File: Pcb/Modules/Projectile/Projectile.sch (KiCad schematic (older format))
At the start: 29 parts, among them J1 JACK_RJ45, Q1 Q_NMOS_GSD, U1 OPA320, U2 OPA320

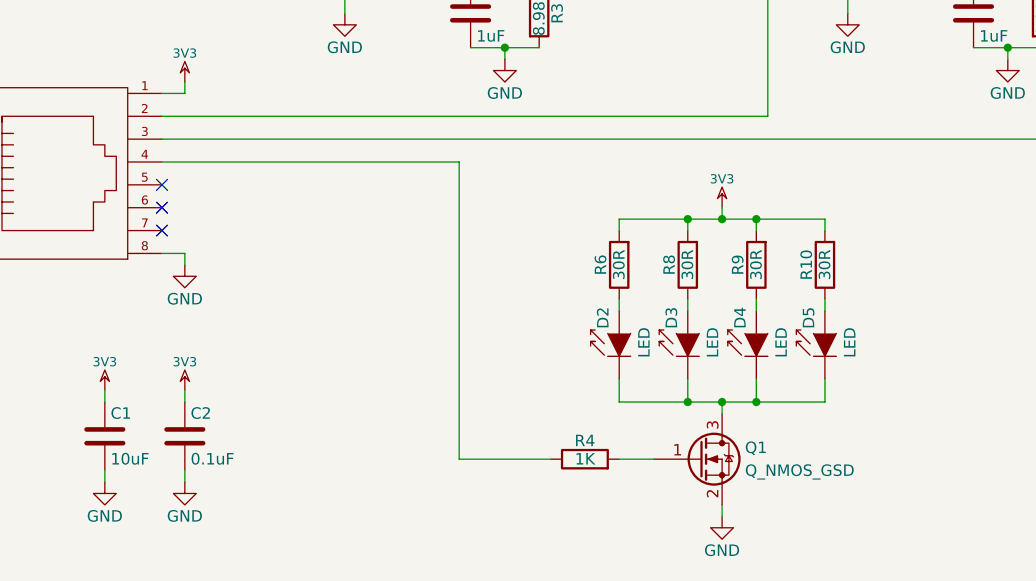
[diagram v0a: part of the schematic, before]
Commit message: Pcb layout for beam and projectile module
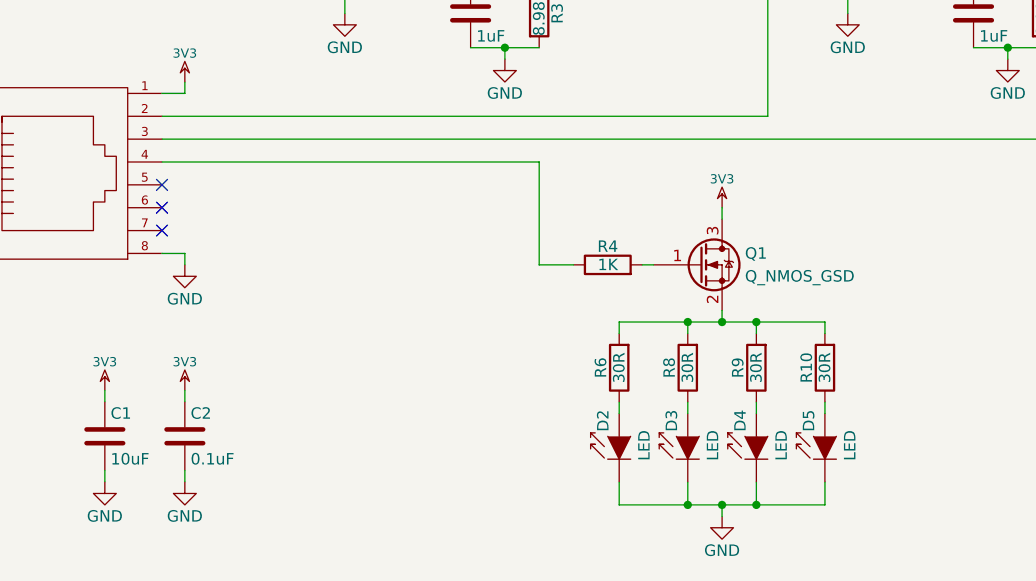
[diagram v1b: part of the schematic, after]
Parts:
- U1, U2: footprint (none) -> TO_SOT_Packages_SMD:SOT-23-5
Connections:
- net 3V3: now also Q1.3 (D); no longer R10.2, R6.2, R8.2, R9.2
- net GND: now also D2.1 (K), D3.1 (K), D4.1 (K), D5.1 (K); no longer Q1.2 (S)
- new net: Q1.2 (S), R10.2, R6.2, R8.2, R9.2
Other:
- moved on the sheet: D2, D3, D4, D5, Q1, R10, R4, R6, R8, R9

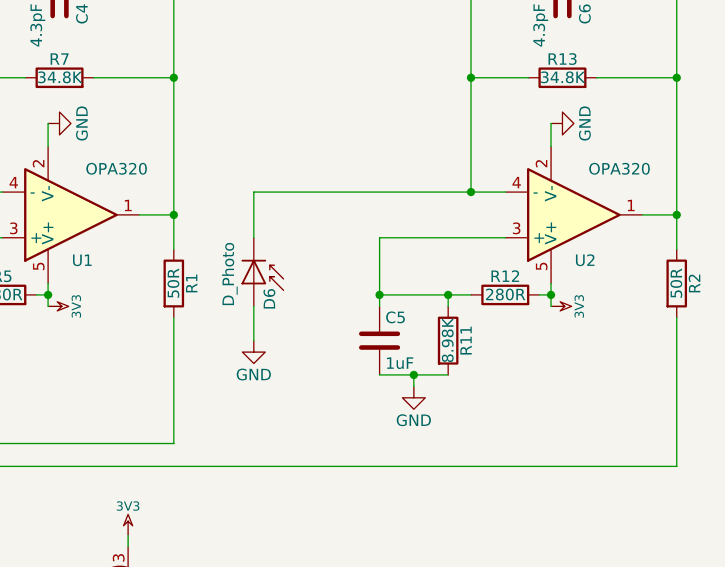
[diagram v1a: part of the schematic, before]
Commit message: Change 50 ohm resistor to 49.9
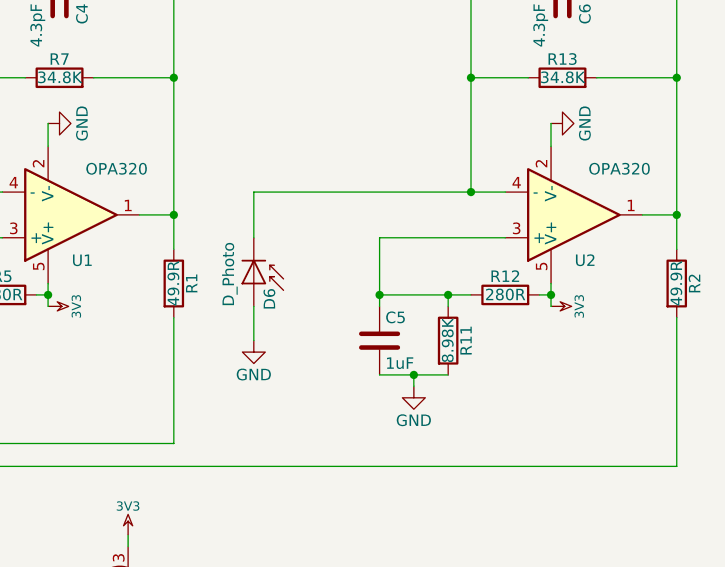
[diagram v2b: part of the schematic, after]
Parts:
- R1, R2: value 50R -> 49.9R
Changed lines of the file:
@@
 P 5300 3200
 F 0 "R1" V 5380 3200 50  0000 C CNN
-F 1 "50R" V 5300 3200 50  0000 C CNN
+F 1 "49.9R" V 5300 3200 50  0000 C CNN
 F 2 "Resistors_SMD:R_0603" V 5230 3200 50  0001 C CNN
 F 3 "" H 5300 3200 50  0001 C CNN
@@
 P 7500 3200
 F 0 "R2" V 7580 3200 50  0000 C CNN
-F 1 "50R" V 7500 3200 50  0000 C CNN
+F 1 "49.9R" V 7500 3200 50  0000 C CNN
 F 2 "Resistors_SMD:R_0603" V 7430 3200 50  0001 C CNN
 F 3 "" H 7500 3200 50  0001 C CNN

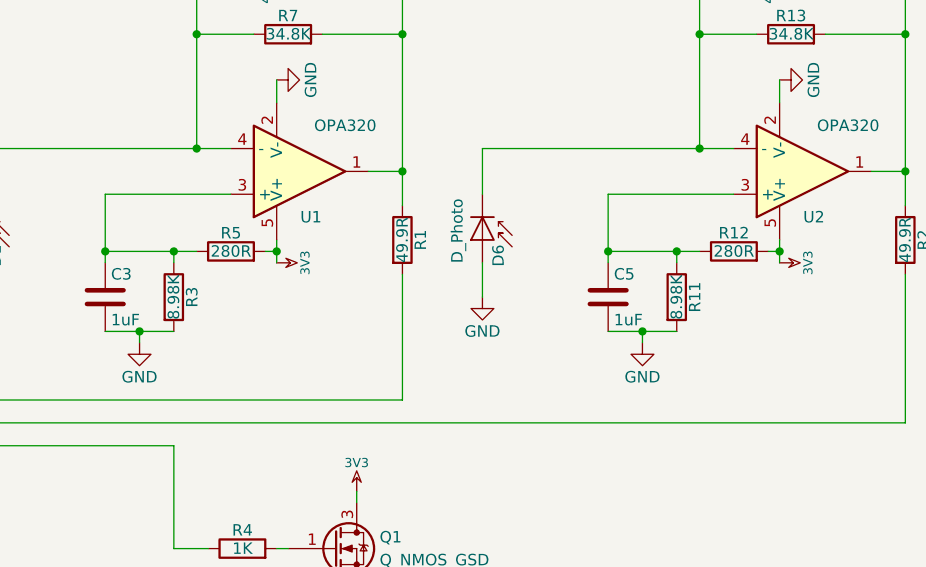
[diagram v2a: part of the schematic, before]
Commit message: Initial projectile menu for testing
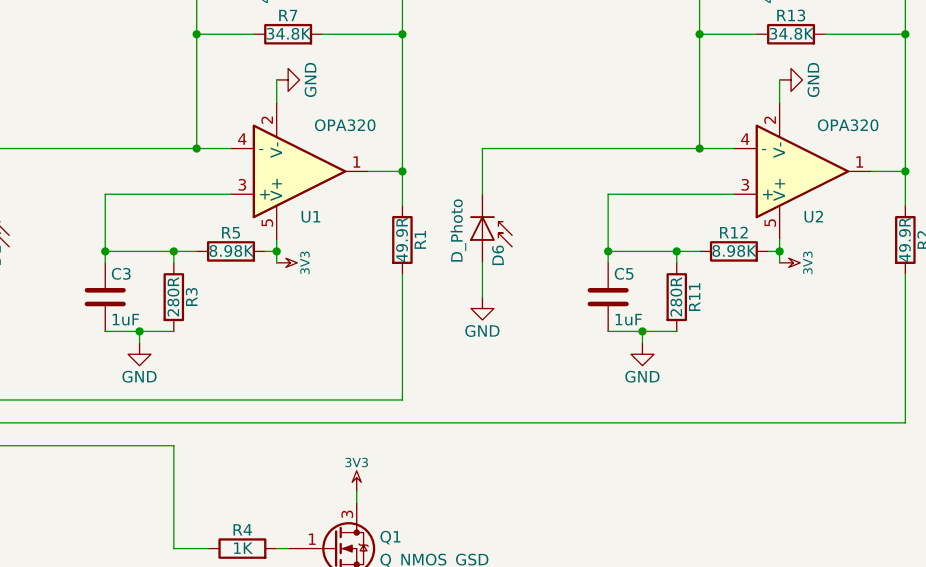
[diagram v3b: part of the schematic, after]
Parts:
- R11, R3: value 8.98K -> 280R
- R12, R5: value 280R -> 8.98K
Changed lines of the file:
@@
 P 4550 3250
 F 0 "R5" V 4630 3250 50  0000 C CNN
-F 1 "280R" V 4550 3250 50  0000 C CNN
+F 1 "8.98K" V 4550 3250 50  0000 C CNN
 F 2 "Resistors_SMD:R_0603" V 4480 3250 50  0001 C CNN
 F 3 "" H 4550 3250 50  0001 C CNN
@@
 P 4300 3450
 F 0 "R3" V 4380 3450 50  0000 C CNN
-F 1 "8.98K" V 4300 3450 50  0000 C CNN
+F 1 "280R" V 4300 3450 50  0000 C CNN
 F 2 "Resistors_SMD:R_0603" V 4230 3450 50  0001 C CNN
 F 3 "" H 4300 3450 50  0001 C CNN
@@
 P 6750 3250
 F 0 "R12" V 6830 3250 50  0000 C CNN
-F 1 "280R" V 6750 3250 50  0000 C CNN
+F 1 "8.98K" V 6750 3250 50  0000 C CNN
 F 2 "Resistors_SMD:R_0603" V 6680 3250 50  0001 C CNN
 F 3 "" H 6750 3250 50  0001 C CNN
@@
 P 6500 3450
 F 0 "R11" V 6580 3450 50  0000 C CNN
-F 1 "8.98K" V 6500 3450 50  0000 C CNN
+F 1 "280R" V 6500 3450 50  0000 C CNN
 F 2 "Resistors_SMD:R_0603" V 6430 3450 50  0001 C CNN
 F 3 "" H 6500 3450 50  0001 C CNN

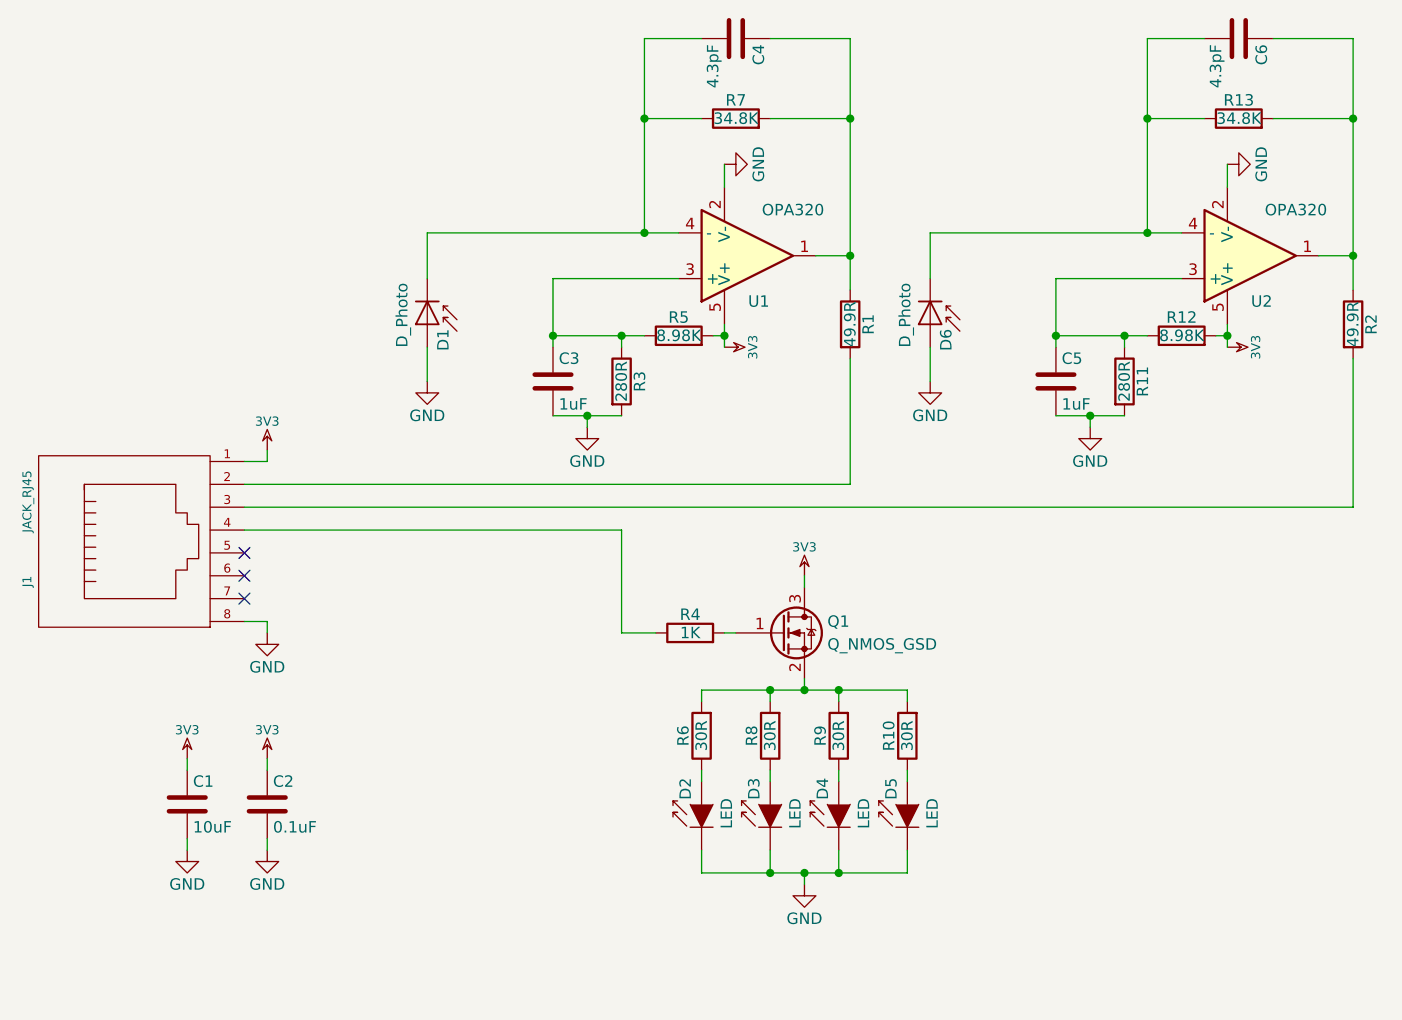
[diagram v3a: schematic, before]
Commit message: Update module pcbs
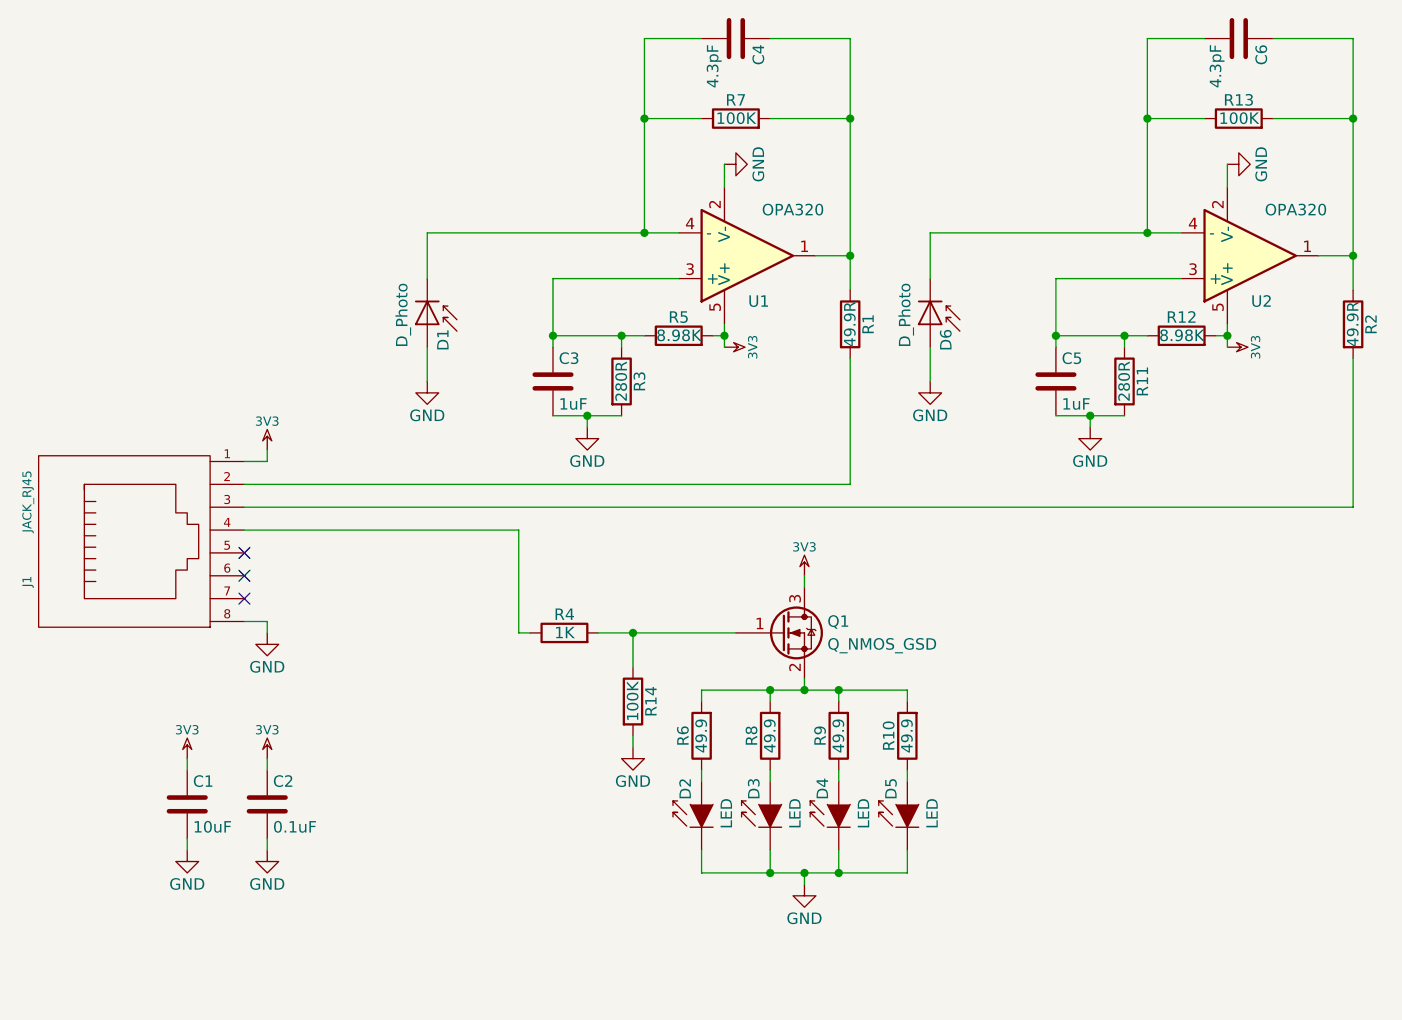
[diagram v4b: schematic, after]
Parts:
- added R14: 100K, Resistors_SMD:R_0603, symbol R
- R10, R6, R8, R9: value 30R -> 49.9
- R13, R7: value 34.8K -> 100K
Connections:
- net GND: now also R14.2
- net at Q1.1 (G), R4.2: now also R14.1
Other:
- moved on the sheet: R4
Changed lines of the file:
@@
 P 4650 5000
 F 0 "R6" V 4730 5000 50  0000 C CNN
-F 1 "30R" V 4650 5000 50  0000 C CNN
+F 1 "49.9" V 4650 5000 50  0000 C CNN
 F 2 "Resistors_SMD:R_0603" V 4580 5000 50  0001 C CNN
 F 3 "" H 4650 5000 50  0001 C CNN
@@
 $EndComp
 $Comp
-L 3V3 #PWR11
+L 3V3 #PWR12
 U 1 1 59FE7828
 P 5100 4300
-F 0 "#PWR11" H 5100 4400 40  0001 C CNN
+F 0 "#PWR12" H 5100 4400 40  0001 C CNN
 F 1 "3V3" H 5100 4425 40  0000 C CNN
 F 2 "" H 5100 4300 60  0000 C CNN
@@
 $EndComp
 $Comp
-L GND #PWR12
+L GND #PWR13
 U 1 1 59FE7854
 P 5100 5650
-F 0 "#PWR12" H 5100 5400 50  0001 C CNN
+F 0 "#PWR13" H 5100 5400 50  0001 C CNN
 F 1 "GND" H 5100 5500 50  0000 C CNN
 F 2 "" H 5100 5650 50  0000 C CNN
@@
 L R R4
 U 1 1 59FE78E6
-P 4600 4550
-F 0 "R4" V 4680 4550 50  0000 C CNN
-F 1 "1K" V 4600 4550 50  0000 C CNN
-F 2 "Resistors_SMD:R_0603" V 4530 4550 50  0001 C CNN
-F 3 "" H 4600 4550 50  0001 C CNN
-	1    4600 4550
+P 4050 4550
+F 0 "R4" V 4130 4550 50  0000 C CNN
+F 1 "1K" V 4050 4550 50  0000 C CNN
+F 2 "Resistors_SMD:R_0603" V 3980 4550 50  0001 C CNN
+F 3 "" H 4050 4550 50  0001 C CNN
+	1    4050 4550
 	0    -1   -1   0
 $EndComp
@@
 $EndComp
 $Comp
-L GND #PWR9
+L GND #PWR10
 U 1 1 59FF5D85
 P 4750 2500
-F 0 "#PWR9" H 4750 2250 50  0001 C CNN
+F 0 "#PWR10" H 4750 2250 50  0001 C CNN
 F 1 "GND" H 4750 2350 50  0000 C CNN
 F 2 "" H 4750 2500 50  0000 C CNN
@@
 $EndComp
 $Comp
-L 3V3 #PWR10
+L 3V3 #PWR11
 U 1 1 59FF6531
 P 4750 3300
-F 0 "#PWR10" H 4750 3400 40  0001 C CNN
+F 0 "#PWR11" H 4750 3400 40  0001 C CNN
 F 1 "3V3" H 4750 3425 40  0000 C CNN
 F 2 "" H 4750 3300 60  0000 C CNN
@@
 P 4800 2300
 F 0 "R7" V 4880 2300 50  0000 C CNN
-F 1 "34.8K" V 4800 2300 50  0000 C CNN
+F 1 "100K" V 4800 2300 50  0000 C CNN
 F 2 "Resistors_SMD:R_0603" V 4730 2300 50  0001 C CNN
 F 3 "" H 4800 2300 50  0001 C CNN
@@
 P 4950 5000
 F 0 "R8" V 5030 5000 50  0000 C CNN
-F 1 "30R" V 4950 5000 50  0000 C CNN
+F 1 "49.9" V 4950 5000 50  0000 C CNN
 F 2 "Resistors_SMD:R_0603" V 4880 5000 50  0001 C CNN
 F 3 "" H 4950 5000 50  0001 C CNN
@@
 P 5250 5000
 F 0 "R9" V 5330 5000 50  0000 C CNN
-F 1 "30R" V 5250 5000 50  0000 C CNN
+F 1 "49.9" V 5250 5000 50  0000 C CNN
 F 2 "Resistors_SMD:R_0603" V 5180 5000 50  0001 C CNN
 F 3 "" H 5250 5000 50  0001 C CNN
@@
 P 5550 5000
 F 0 "R10" V 5630 5000 50  0000 C CNN
-F 1 "30R" V 5550 5000 50  0000 C CNN
+F 1 "49.9" V 5550 5000 50  0000 C CNN
 F 2 "Resistors_SMD:R_0603" V 5480 5000 50  0001 C CNN
 F 3 "" H 5550 5000 50  0001 C CNN
@@
 Connection ~ 4950 5600
 Wire Wire Line
-	2650 4100 4300 4100
+	2650 4100 3850 4100
 $Comp
 L MCP601 U2
@@
 $EndComp
 $Comp
-L GND #PWR15
+L GND #PWR16
 U 1 1 5A000C0A
 P 6950 2500
-F 0 "#PWR15" H 6950 2250 50  0001 C CNN
+F 0 "#PWR16" H 6950 2250 50  0001 C CNN
 F 1 "GND" H 6950 2350 50  0000 C CNN
 F 2 "" H 6950 2500 50  0000 C CNN
@@
 $EndComp
 $Comp
-L 3V3 #PWR16
+L 3V3 #PWR17
 U 1 1 5A000C10
 P 6950 3300
-F 0 "#PWR16" H 6950 3400 40  0001 C CNN
+F 0 "#PWR17" H 6950 3400 40  0001 C CNN
 F 1 "3V3" H 6950 3425 40  0000 C CNN
 F 2 "" H 6950 3300 60  0000 C CNN
@@
 $EndComp
 $Comp
-L GND #PWR14
+L GND #PWR15
 U 1 1 5A000C28
 P 6350 3650
-F 0 "#PWR14" H 6350 3400 50  0001 C CNN
+F 0 "#PWR15" H 6350 3400 50  0001 C CNN
 F 1 "GND" H 6350 3500 50  0000 C CNN
 F 2 "" H 6350 3650 50  0000 C CNN
@@
 P 7000 2300
 F 0 "R13" V 7080 2300 50  0000 C CNN
-F 1 "34.8K" V 7000 2300 50  0000 C CNN
+F 1 "100K" V 7000 2300 50  0000 C CNN
 F 2 "Resistors_SMD:R_0603" V 6930 2300 50  0001 C CNN
 F 3 "" H 7000 2300 50  0001 C CNN
@@
 $EndComp
 $Comp
-L GND #PWR13
+L GND #PWR14
 U 1 1 5A000C59
 P 5650 3450
-F 0 "#PWR13" H 5650 3200 50  0001 C CNN
+F 0 "#PWR14" H 5650 3200 50  0001 C CNN
 F 1 "GND" H 5650 3300 50  0000 C CNN
 F 2 "" H 5650 3450 50  0000 C CNN
@@
 	5100 4300 5100 4350
 Wire Wire Line
-	4800 4550 4750 4550
-Wire Wire Line
-	4450 4550 4300 4550
-Wire Wire Line
-	4300 4550 4300 4100
+	4800 4550 4200 4550
+Wire Wire Line
+	3900 4550 3850 4550
+Wire Wire Line
+	3850 4550 3850 4100
+$Comp
+L R R14
+U 1 1 5A220CAD
+P 4350 4850
+F 0 "R14" V 4430 4850 50  0000 C CNN
+F 1 "100K" V 4350 4850 50  0000 C CNN
+F 2 "Resistors_SMD:R_0603" V 4280 4850 50  0001 C CNN
+F 3 "" H 4350 4850 50  0001 C CNN
+	1    4350 4850
+	1    0    0    -1
+$EndComp
+Wire Wire Line
+	4350 4700 4350 4550
+Connection ~ 4350 4550
+$Comp
+L GND #PWR9
+U 1 1 5A2210AC
+P 4350 5050
+F 0 "#PWR9" H 4350 4800 50  0001 C CNN
+F 1 "GND" H 4350 4900 50  0000 C CNN
+F 2 "" H 4350 5050 50  0000 C CNN
+F 3 "" H 4350 5050 50  0000 C CNN
+	1    4350 5050
+	1    0    0    -1
+$EndComp
+Wire Wire Line
+	4350 5000 4350 5050
 $EndSCHEMATC

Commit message: Update PCBs
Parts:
- added X1, X2, X3, X4: HOLE, Mounting_Holes:MountingHole_2.5mm_Pad, symbol HOLE
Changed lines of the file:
@@
 Wire Wire Line
 	4350 5000 4350 5050
+$Comp
+L HOLE X1
+U 1 1 5A235115
+P 3450 5950
+F 0 "X1" H 3450 5850 60  0000 C CNN
+F 1 "HOLE" H 3450 6050 60  0000 C CNN
+F 2 "Mounting_Holes:MountingHole_2.5mm_Pad" H 3450 5950 60  0001 C CNN
+F 3 "" H 3450 5950 60  0000 C CNN
+	1    3450 5950
+	1    0    0    -1
+$EndComp
+$Comp
+L HOLE X2
+U 1 1 5A235277
+P 3750 5950
+F 0 "X2" H 3750 5850 60  0000 C CNN
+F 1 "HOLE" H 3750 6050 60  0000 C CNN
+F 2 "Mounting_Holes:MountingHole_2.5mm_Pad" H 3750 5950 60  0001 C CNN
+F 3 "" H 3750 5950 60  0000 C CNN
+	1    3750 5950
+	1    0    0    -1
+$EndComp
+$Comp
+L HOLE X3
+U 1 1 5A2352EF
+P 4050 5950
+F 0 "X3" H 4050 5850 60  0000 C CNN
+F 1 "HOLE" H 4050 6050 60  0000 C CNN
+F 2 "Mounting_Holes:MountingHole_2.5mm_Pad" H 4050 5950 60  0001 C CNN
+F 3 "" H 4050 5950 60  0000 C CNN
+	1    4050 5950
+	1    0    0    -1
+$EndComp
+$Comp
+L HOLE X4
+U 1 1 5A23536A
+P 4350 5950
+F 0 "X4" H 4350 5850 60  0000 C CNN
+F 1 "HOLE" H 4350 6050 60  0000 C CNN
+F 2 "Mounting_Holes:MountingHole_2.5mm_Pad" H 4350 5950 60  0001 C CNN
+F 3 "" H 4350 5950 60  0000 C CNN
+	1    4350 5950
+	1    0    0    -1
+$EndComp
 $EndSCHEMATC
